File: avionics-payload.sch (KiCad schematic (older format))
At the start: 27 parts, among them J1 Conn_Coaxial_x2, SW1 SW_Push, SW2 SW_Push, U1 ADXL357BEZ, U2 Teensy4.0, U3 RFM96W-433S2, U4 ublox_SAM-M8Q, U5 MS5607-02BA

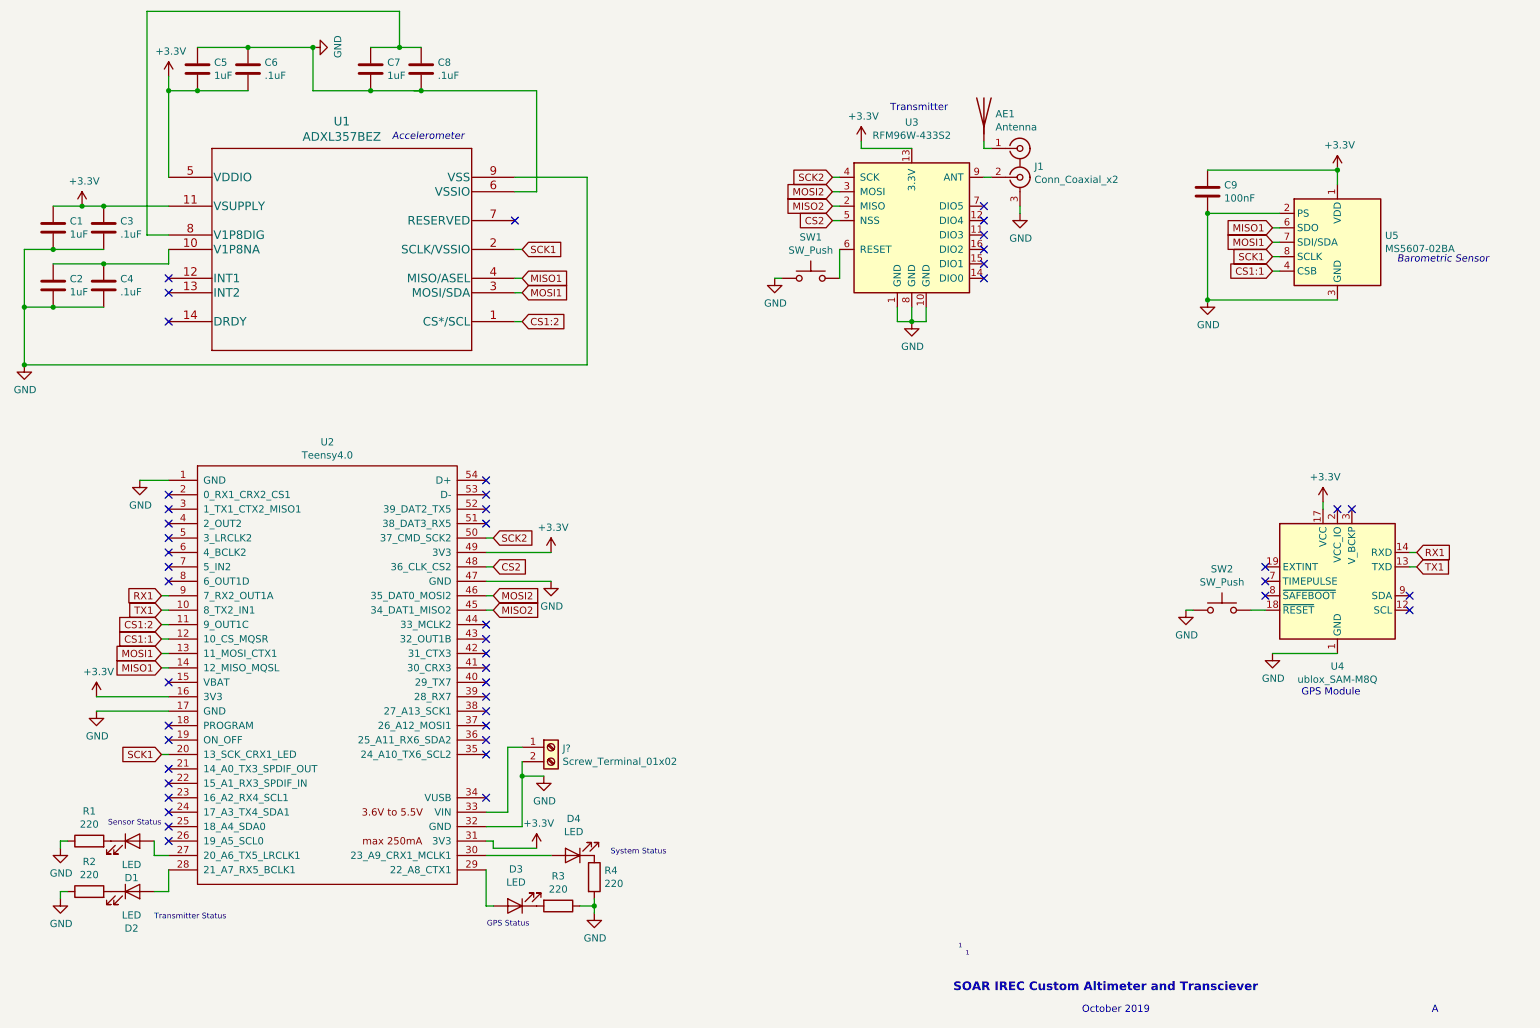
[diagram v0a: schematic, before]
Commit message: Added power module and made schematic more modular.
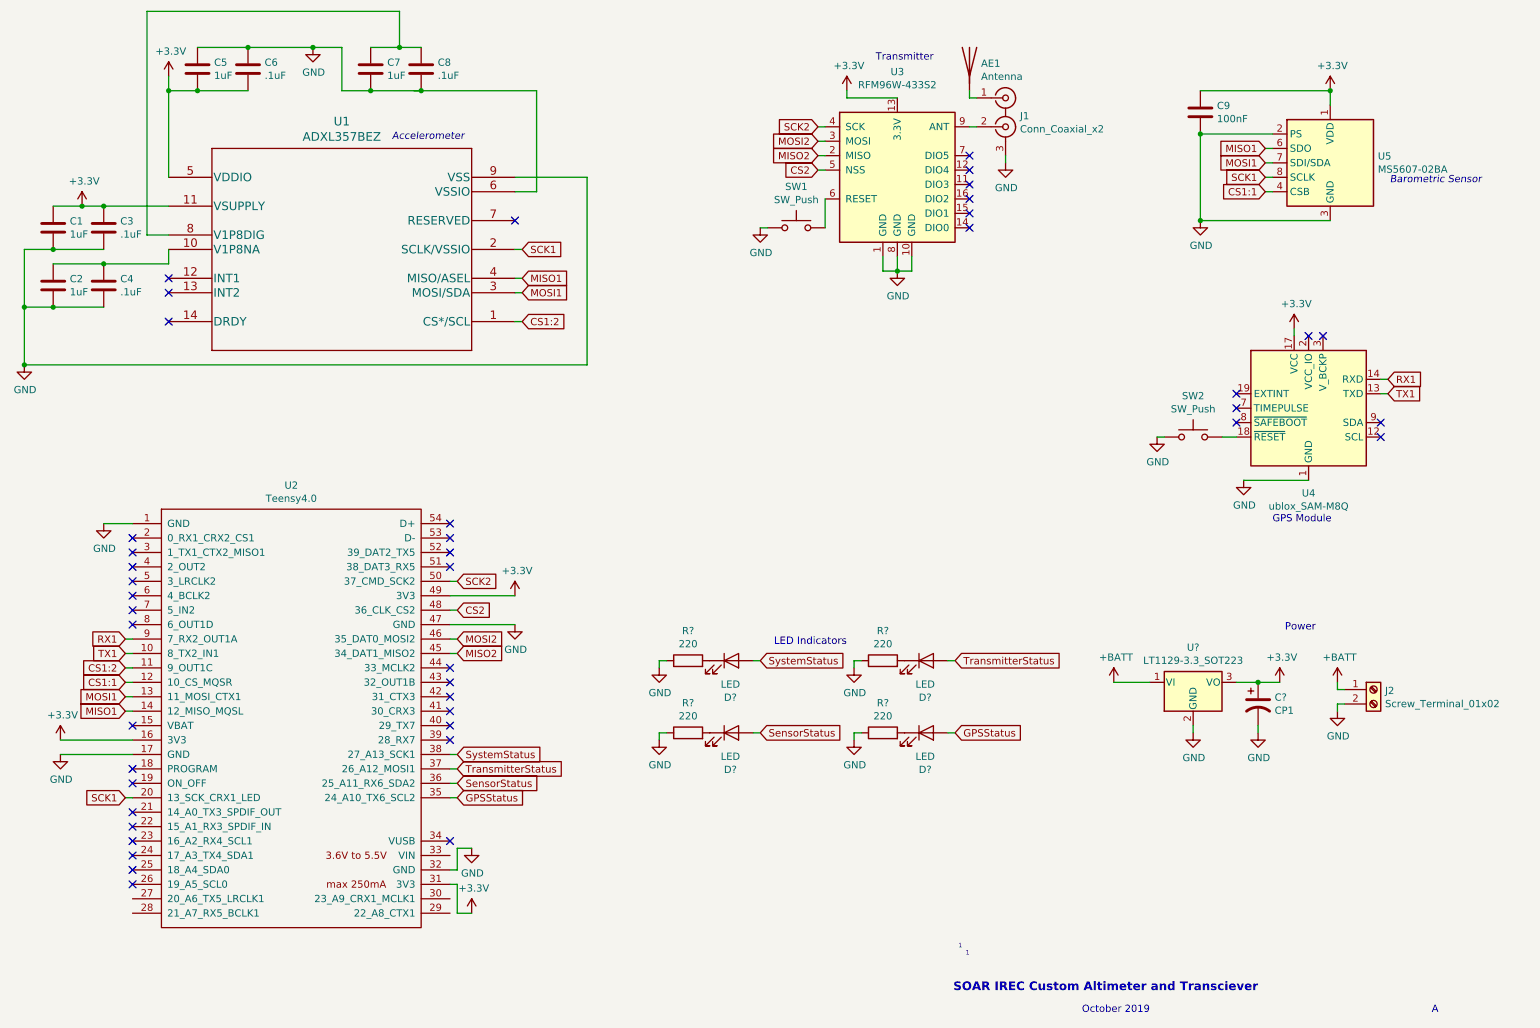
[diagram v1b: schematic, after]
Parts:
- removed D1, D2, D3, D4: LED, LED_SMD:LED_1206_3216Metric_Pad1.42x1.75mm_HandSolder, symbol Device:LED
- removed R1, R2, R3, R4: 220, Resistor_SMD:R_0805_2012Metric_Pad1.15x1.40mm_HandSolder, symbol Device:R
- added C?: CP1, symbol Device:CP1
- added D? (x4): LED, LED_SMD:LED_1206_3216Metric_Pad1.42x1.75mm_HandSolder, symbol Device:LED
- added R? (x4): 220, Resistor_SMD:R_0805_2012Metric_Pad1.15x1.40mm_HandSolder, symbol Device:R
- added U?: LT1129-3.3_SOT223, Package_TO_SOT_SMD:SOT-223-3_TabPin2, symbol Regulator_Linear:LT1129-3.3_SOT223
- gave numbers to parts that had none: 1
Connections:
- net +3V3: now also C?.1, U?.3 (VO)
- net GND: now also C?.2, R?.1, R?.1, R?.1, R?.1, U?.2 (GND)
- net at U2.33 (VIN): no longer J2.1 (Pin_1)
- net GPSStatus: now reaches U2.35 (24_A10_TX6_SCL2)
- net GPSStatus: now also D?.2 (A)
- net SensorStatus: now reaches U2.36 (25_A11_RX6_SDA2)
- net SensorStatus: now also D?.2 (A)
- net TransmitterStatus: now reaches U2.37 (26_A12_MOSI1)
- net TransmitterStatus: now also D?.2 (A)
- net SystemStatus: now reaches U2.38 (27_A13_SCK1)
- net SystemStatus: now also D?.2 (A)
- new net: D?.1 (K), R?.2 (x4)
- new net +BATT: J2.1 (Pin_1), U?.1 (VI)
- no-connect marks 48 -> 44
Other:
- note added: "LED Indicators"
- note added: "Power"
- note removed: "GPS Status\n"
- note removed: "Sensor Status\n"
- note removed: "System Status\n"
- note removed: "Transmitter Status\n"
- moved on the sheet: AE1, C9, J1, J2, SW1, SW2, U2, U3, U4, U5
